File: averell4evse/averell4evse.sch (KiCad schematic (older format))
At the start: 23 parts, among them J1 Conn_01x16, J2 Conn_01x12, J3 Conn_01x04, U1 KT2520K-T, U2 NFCv4, U3 TLC5957RTQ, U4 74AUC1G126, U5 touch_sensor

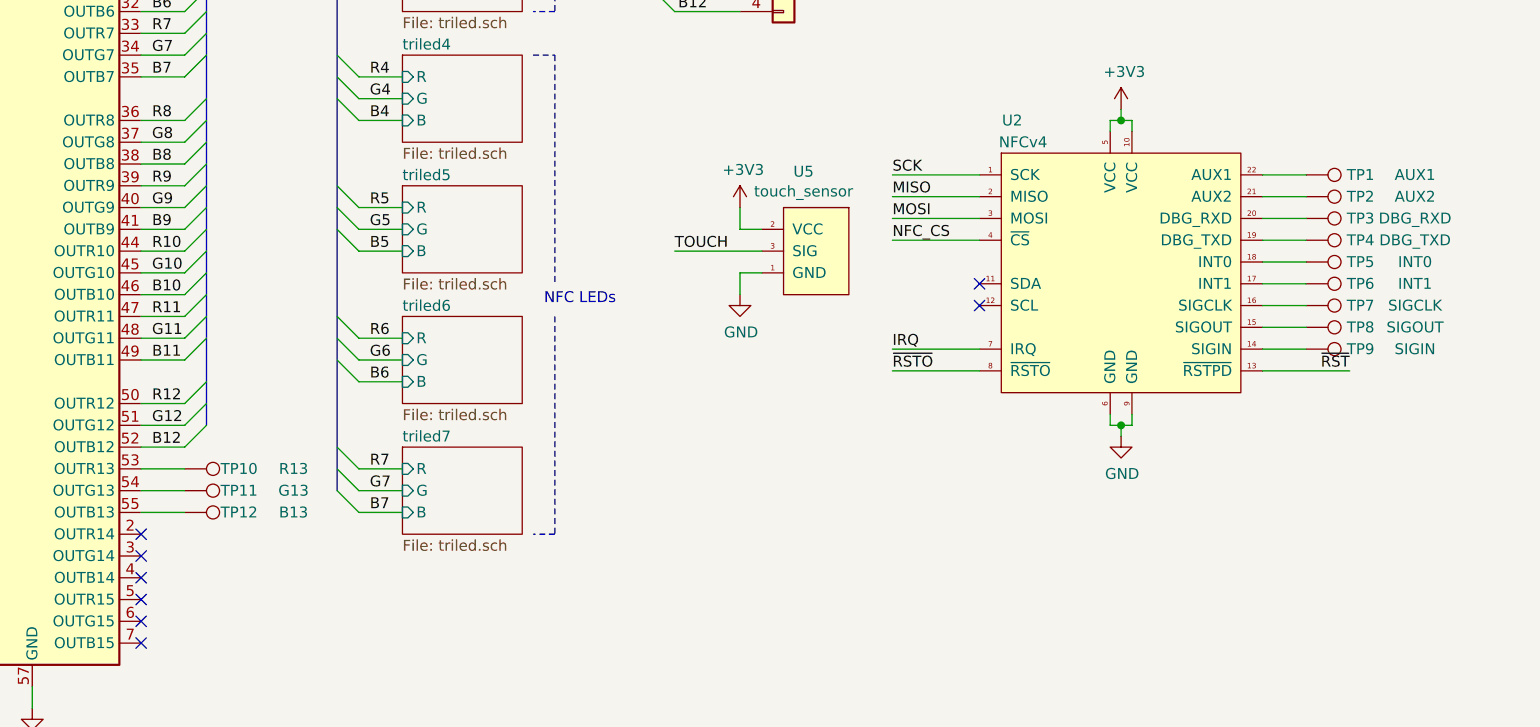
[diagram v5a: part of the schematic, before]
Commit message: averell: Replace test pads with 0.1" pin headers
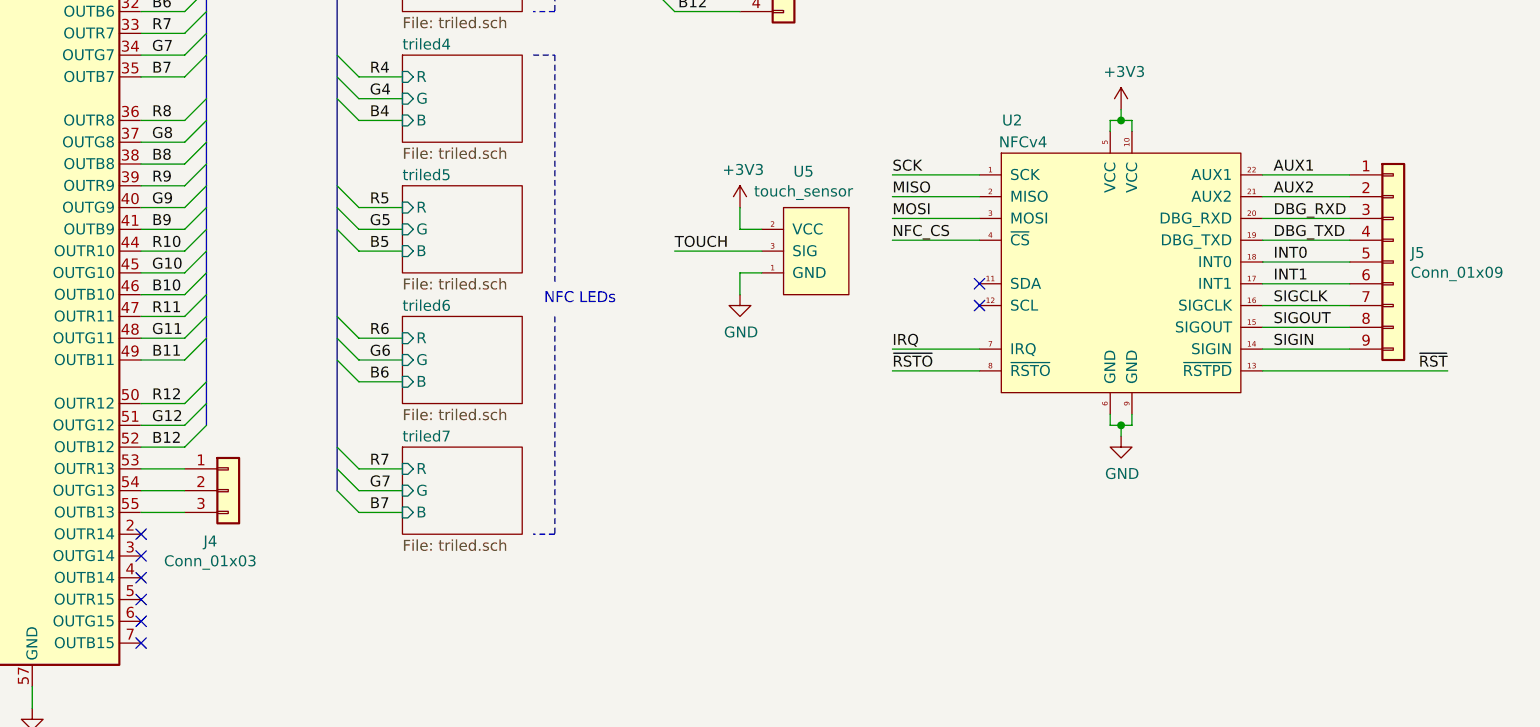
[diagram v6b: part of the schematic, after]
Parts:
- removed TP1: AUX1, TestPoint:TestPoint_THTPad_D1.0mm_Drill0.5mm, symbol Connector:TestPoint
- removed TP10: R13, TestPoint:TestPoint_THTPad_D1.0mm_Drill0.5mm, symbol Connector:TestPoint
- removed TP11: G13, TestPoint:TestPoint_THTPad_D1.0mm_Drill0.5mm, symbol Connector:TestPoint
- removed TP12: B13, TestPoint:TestPoint_THTPad_D1.0mm_Drill0.5mm, symbol Connector:TestPoint
- removed TP2: AUX2, TestPoint:TestPoint_THTPad_D1.0mm_Drill0.5mm, symbol Connector:TestPoint
- removed TP3: DBG_RXD, TestPoint:TestPoint_THTPad_D1.0mm_Drill0.5mm, symbol Connector:TestPoint
- removed TP4: DBG_TXD, TestPoint:TestPoint_THTPad_D1.0mm_Drill0.5mm, symbol Connector:TestPoint
- removed TP5: INT0, TestPoint:TestPoint_THTPad_D1.0mm_Drill0.5mm, symbol Connector:TestPoint
- removed TP6: INT1, TestPoint:TestPoint_THTPad_D1.0mm_Drill0.5mm, symbol Connector:TestPoint
- removed TP7: SIGCLK, TestPoint:TestPoint_THTPad_D1.0mm_Drill0.5mm, symbol Connector:TestPoint
- removed TP8: SIGOUT, TestPoint:TestPoint_THTPad_D1.0mm_Drill0.5mm, symbol Connector:TestPoint
- removed TP9: SIGIN, TestPoint:TestPoint_THTPad_D1.0mm_Drill0.5mm, symbol Connector:TestPoint
- added J4: Conn_01x03, Connector_PinHeader_2.54mm:PinHeader_1x03_P2.54mm_Horizontal, symbol Connector_Generic:Conn_01x03
- added J5: Conn_01x09, Connector_PinHeader_2.54mm:PinHeader_1x09_P2.54mm_Horizontal, symbol Connector_Generic:Conn_01x09
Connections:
- net at U3.53 (OUTR13): now also J4.1 (Pin_1)
- net at U3.54 (OUTG13): now also J4.2 (Pin_2)
- net at U3.55 (OUTB13): now also J4.3 (Pin_3)
- net SIGIN: now reaches U2.14 (SIGIN)
- net SIGIN: now also J5.9 (Pin_9)
- net SIGOUT: now reaches U2.15 (SIGOUT)
- net SIGOUT: now also J5.8 (Pin_8)
- net SIGCLK: now reaches U2.16 (SIGCLK)
- net SIGCLK: now also J5.7 (Pin_7)
- net INT1: now reaches U2.17 (INT1)
- net INT1: now also J5.6 (Pin_6)
- net INT0: now reaches U2.18 (INT0)
- net INT0: now also J5.5 (Pin_5)
- net DBG_TXD: now reaches U2.19 (DBG_TXD)
- net DBG_TXD: now also J5.4 (Pin_4)
- net DBG_RXD: now reaches U2.20 (DBG_RXD)
- net DBG_RXD: now also J5.3 (Pin_3)
- net AUX2: now reaches U2.21 (AUX2)
- net AUX2: now also J5.2 (Pin_2)
- net AUX1: now reaches U2.22 (AUX1)
- net AUX1: now also J5.1 (Pin_1)
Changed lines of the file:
@@
 EESchema Schematic File Version 4
+LIBS:averell4evse-cache
 EELAYER 29 0
 EELAYER END
@@
 	3050 4350 3050 4300
 Wire Wire Line
-	10050 5200 10450 5200
-Text Label 10450 5200 2    50   ~ 0
+	10050 5200 10900 5200
+Text Label 10900 5200 2    50   ~ 0
 ~RST
 $Comp
@@
 The LED driver has no chip select pin,\nthus its SOUT pin never goes high-Z.\nFor a shared MISO, inactive devices must\nput their MISO pin in high-Z, which we\nsimulate here with the buffer chip.
 Wire Wire Line
-	10050 4300 10250 4300
+	10050 4300 10450 4300
 $Comp
 L ma4evse:NFCv4 U2
@@
 	1    0    0    -1
 $EndComp
-$Comp
-L Connector:TestPoint TP1
-U 1 1 5DEAD7B1
-P 10250 4300
-F 0 "TP1" V 10250 4550 50  0000 C CNN
-F 1 "AUX1" V 10250 4800 50  0000 C CNN
-F 2 "TestPoint:TestPoint_THTPad_D1.0mm_Drill0.5mm" H 10450 4300 50  0001 C CNN
-F 3 "~" H 10450 4300 50  0001 C CNN
-	1    10250 4300
-	0    1    1    0
-$EndComp
-Wire Wire Line
-	10050 4400 10250 4400
-$Comp
-L Connector:TestPoint TP2
-U 1 1 5DF04769
-P 10250 4400
-F 0 "TP2" V 10250 4650 50  0000 C CNN
-F 1 "AUX2" V 10250 4900 50  0000 C CNN
-F 2 "TestPoint:TestPoint_THTPad_D1.0mm_Drill0.5mm" H 10450 4400 50  0001 C CNN
-F 3 "~" H 10450 4400 50  0001 C CNN
-	1    10250 4400
-	0    1    1    0
-$EndComp
-Wire Wire Line
-	10050 4500 10250 4500
-$Comp
-L Connector:TestPoint TP3
-U 1 1 5DF0C8F8
-P 10250 4500
-F 0 "TP3" V 10250 4750 50  0000 C CNN
-F 1 "DBG_RXD" V 10250 5000 50  0000 C CNN
-F 2 "TestPoint:TestPoint_THTPad_D1.0mm_Drill0.5mm" H 10450 4500 50  0001 C CNN
-F 3 "~" H 10450 4500 50  0001 C CNN
-	1    10250 4500
-	0    1    1    0
-$EndComp
-Wire Wire Line
-	10050 4600 10250 4600
-$Comp
-L Connector:TestPoint TP4
-U 1 1 5DF14B53
-P 10250 4600
-F 0 "TP4" V 10250 4850 50  0000 C CNN
-F 1 "DBG_TXD" V 10250 5100 50  0000 C CNN
-F 2 "TestPoint:TestPoint_THTPad_D1.0mm_Drill0.5mm" H 10450 4600 50  0001 C CNN
-F 3 "~" H 10450 4600 50  0001 C CNN
-	1    10250 4600
-	0    1    1    0
-$EndComp
-Wire Wire Line
-	10050 4700 10250 4700
-$Comp
-L Connector:TestPoint TP5
-U 1 1 5DF1CF0D
-P 10250 4700
-F 0 "TP5" V 10250 4950 50  0000 C CNN
-F 1 "INT0" V 10250 5200 50  0000 C CNN
-F 2 "TestPoint:TestPoint_THTPad_D1.0mm_Drill0.5mm" H 10450 4700 50  0001 C CNN
-F 3 "~" H 10450 4700 50  0001 C CNN
-	1    10250 4700
-	0    1    1    0
-$EndComp
-Wire Wire Line
-	10050 4800 10250 4800
-$Comp
-L Connector:TestPoint TP6
-U 1 1 5DF253F3
-P 10250 4800
-F 0 "TP6" V 10250 5050 50  0000 C CNN
-F 1 "INT1" V 10250 5300 50  0000 C CNN
-F 2 "TestPoint:TestPoint_THTPad_D1.0mm_Drill0.5mm" H 10450 4800 50  0001 C CNN
-F 3 "~" H 10450 4800 50  0001 C CNN
-	1    10250 4800
-	0    1    1    0
-$EndComp
-Wire Wire Line
-	10050 4900 10250 4900
-$Comp
-L Connector:TestPoint TP7
-U 1 1 5DF2DAFE
-P 10250 4900
-F 0 "TP7" V 10250 5150 50  0000 C CNN
-F 1 "SIGCLK" V 10250 5400 50  0000 C CNN
-F 2 "TestPoint:TestPoint_THTPad_D1.0mm_Drill0.5mm" H 10450 4900 50  0001 C CNN
-F 3 "~" H 10450 4900 50  0001 C CNN
-	1    10250 4900
-	0    1    1    0
-$EndComp
-Wire Wire Line
-	10050 5000 10250 5000
-$Comp
-L Connector:TestPoint TP8
-U 1 1 5DF363A1
-P 10250 5000
-F 0 "TP8" V 10250 5250 50  0000 C CNN
-F 1 "SIGOUT" V 10250 5500 50  0000 C CNN
-F 2 "TestPoint:TestPoint_THTPad_D1.0mm_Drill0.5mm" H 10450 5000 50  0001 C CNN
-F 3 "~" H 10450 5000 50  0001 C CNN
-	1    10250 5000
-	0    1    1    0
-$EndComp
-Wire Wire Line
-	10050 5100 10250 5100
-$Comp
-L Connector:TestPoint TP9
-U 1 1 5DF3ED31
-P 10250 5100
-F 0 "TP9" V 10250 5350 50  0000 C CNN
-F 1 "SIGIN" V 10250 5600 50  0000 C CNN
-F 2 "TestPoint:TestPoint_THTPad_D1.0mm_Drill0.5mm" H 10450 5100 50  0001 C CNN
-F 3 "~" H 10450 5100 50  0001 C CNN
-	1    10250 5100
-	0    1    1    0
-$EndComp
+Wire Wire Line
+	10050 4400 10450 4400
+Wire Wire Line
+	10050 4500 10450 4500
+Wire Wire Line
+	10050 4600 10450 4600
+Wire Wire Line
+	10050 4700 10450 4700
+Wire Wire Line
+	10050 4800 10450 4800
+Wire Wire Line
+	10050 4900 10450 4900
+Wire Wire Line
+	10050 5000 10450 5000
+Wire Wire Line
+	10050 5100 10450 5100
 Wire Wire Line
 	4900 5650 5100 5650
-$Comp
-L Connector:TestPoint TP10
-U 1 1 5DF480E2
-P 5100 5650
-F 0 "TP10" V 5100 5900 50  0000 C CNN
-F 1 "R13" V 5100 6150 50  0000 C CNN
-F 2 "TestPoint:TestPoint_THTPad_D1.0mm_Drill0.5mm" H 5300 5650 50  0001 C CNN
-F 3 "~" H 5300 5650 50  0001 C CNN
-	1    5100 5650
-	0    1    1    0
-$EndComp
 Wire Wire Line
 	4900 5750 5100 5750
-$Comp
-L Connector:TestPoint TP11
-U 1 1 5DF480E9
-P 5100 5750
-F 0 "TP11" V 5100 6000 50  0000 C CNN
-F 1 "G13" V 5100 6250 50  0000 C CNN
-F 2 "TestPoint:TestPoint_THTPad_D1.0mm_Drill0.5mm" H 5300 5750 50  0001 C CNN
-F 3 "~" H 5300 5750 50  0001 C CNN
-	1    5100 5750
-	0    1    1    0
-$EndComp
 Wire Wire Line
 	4900 5850 5100 5850
-$Comp
-L Connector:TestPoint TP12
-U 1 1 5DF480F0
-P 5100 5850
-F 0 "TP12" V 5100 6100 50  0000 C CNN
-F 1 "B13" V 5100 6350 50  0000 C CNN
-F 2 "TestPoint:TestPoint_THTPad_D1.0mm_Drill0.5mm" H 5300 5850 50  0001 C CNN
-F 3 "~" H 5300 5850 50  0001 C CNN
-	1    5100 5850
-	0    1    1    0
-$EndComp
 $Sheet
 S 6100 1950 550  400
@@
 	1    0    0    -1
 $EndComp
+$Comp
+L Connector_Generic:Conn_01x03 J4
+U 1 1 5DDA55B8
+P 5300 5750
+F 0 "J4" H 5218 5517 50  0000 C CNN
+F 1 "Conn_01x03" H 5218 5426 50  0000 C CNN
+F 2 "Connector_PinHeader_2.54mm:PinHeader_1x03_P2.54mm_Horizontal" H 5300 5750 50  0001 C CNN
+F 3 "~" H 5300 5750 50  0001 C CNN
+	1    5300 5750
+	1    0    0    -1
+$EndComp
+$Comp
+L Connector_Generic:Conn_01x09 J5
+U 1 1 5DDB2582
+P 10650 4700
+F 0 "J5" H 10730 4742 50  0000 L CNN
+F 1 "Conn_01x09" H 10730 4651 50  0000 L CNN
+F 2 "Connector_PinHeader_2.54mm:PinHeader_1x09_P2.54mm_Horizontal" H 10650 4700 50  0001 C CNN
+F 3 "~" H 10650 4700 50  0001 C CNN
+	1    10650 4700
+	1    0    0    -1
+$EndComp
+Text Label 10100 4300 0    50   ~ 0
+AUX1
+Text Label 10100 4400 0    50   ~ 0
+AUX2
+Text Label 10100 4500 0    50   ~ 0
+DBG_RXD
+Text Label 10100 4600 0    50   ~ 0
+DBG_TXD
+Text Label 10100 4700 0    50   ~ 0
+INT0
+Text Label 10100 4800 0    50   ~ 0
+INT1
+Text Label 10100 4900 0    50   ~ 0
+SIGCLK
+Text Label 10100 5000 0    50   ~ 0
+SIGOUT
+Text Label 10100 5100 0    50   ~ 0
+SIGIN
 Wire Bus Line
 	7250 1050 7250 3450

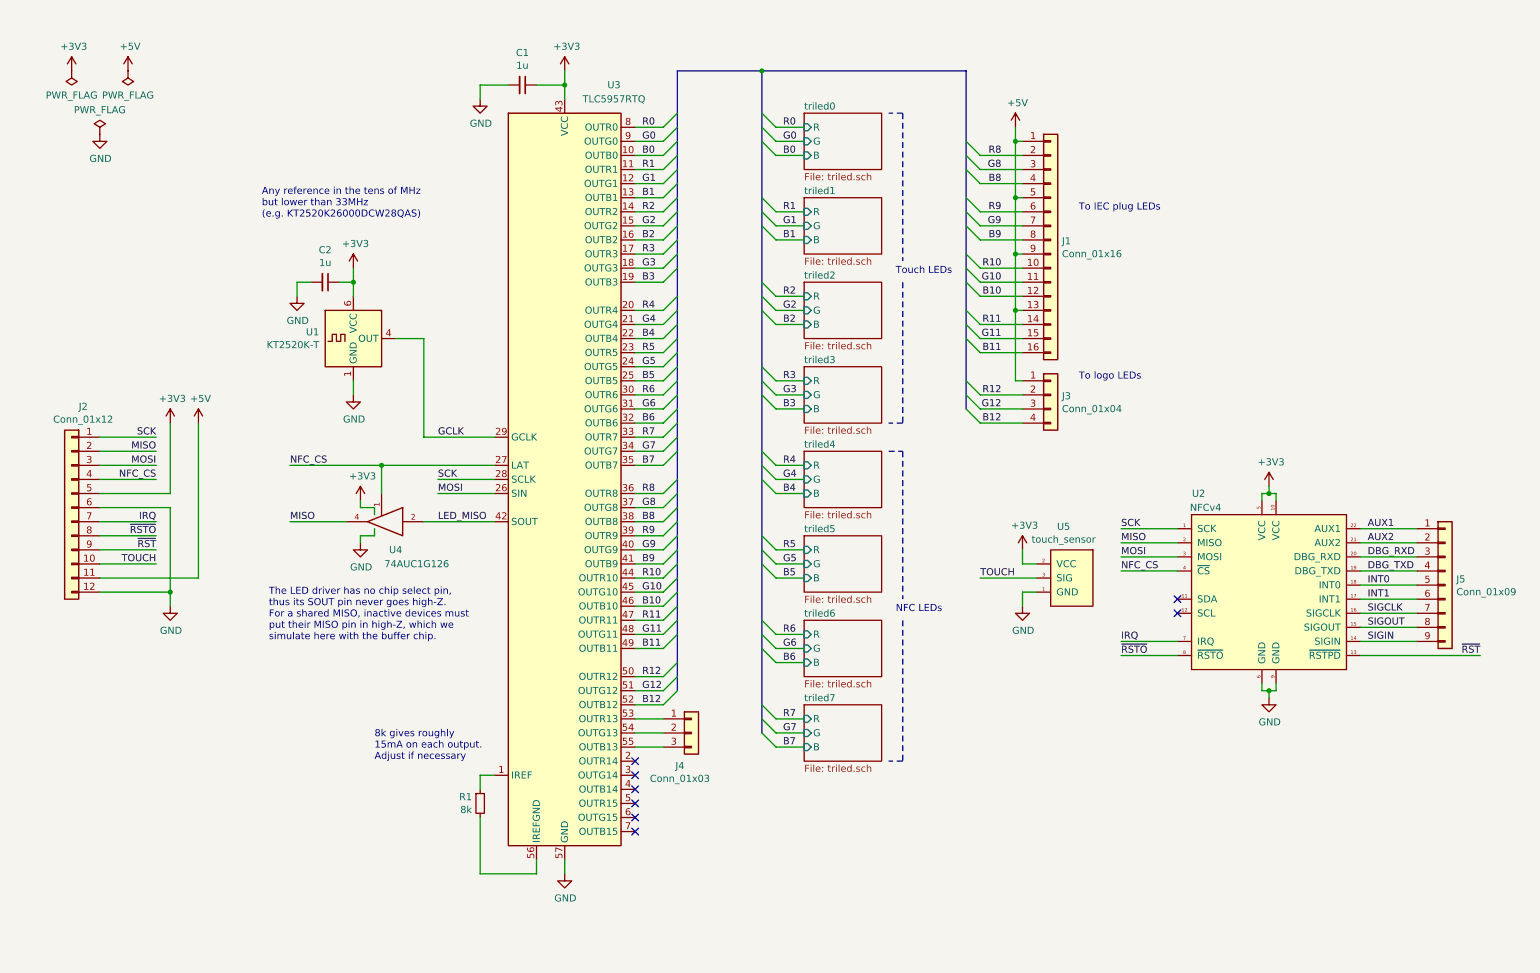
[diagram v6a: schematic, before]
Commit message: averell/*: Make a real CS for LED driver
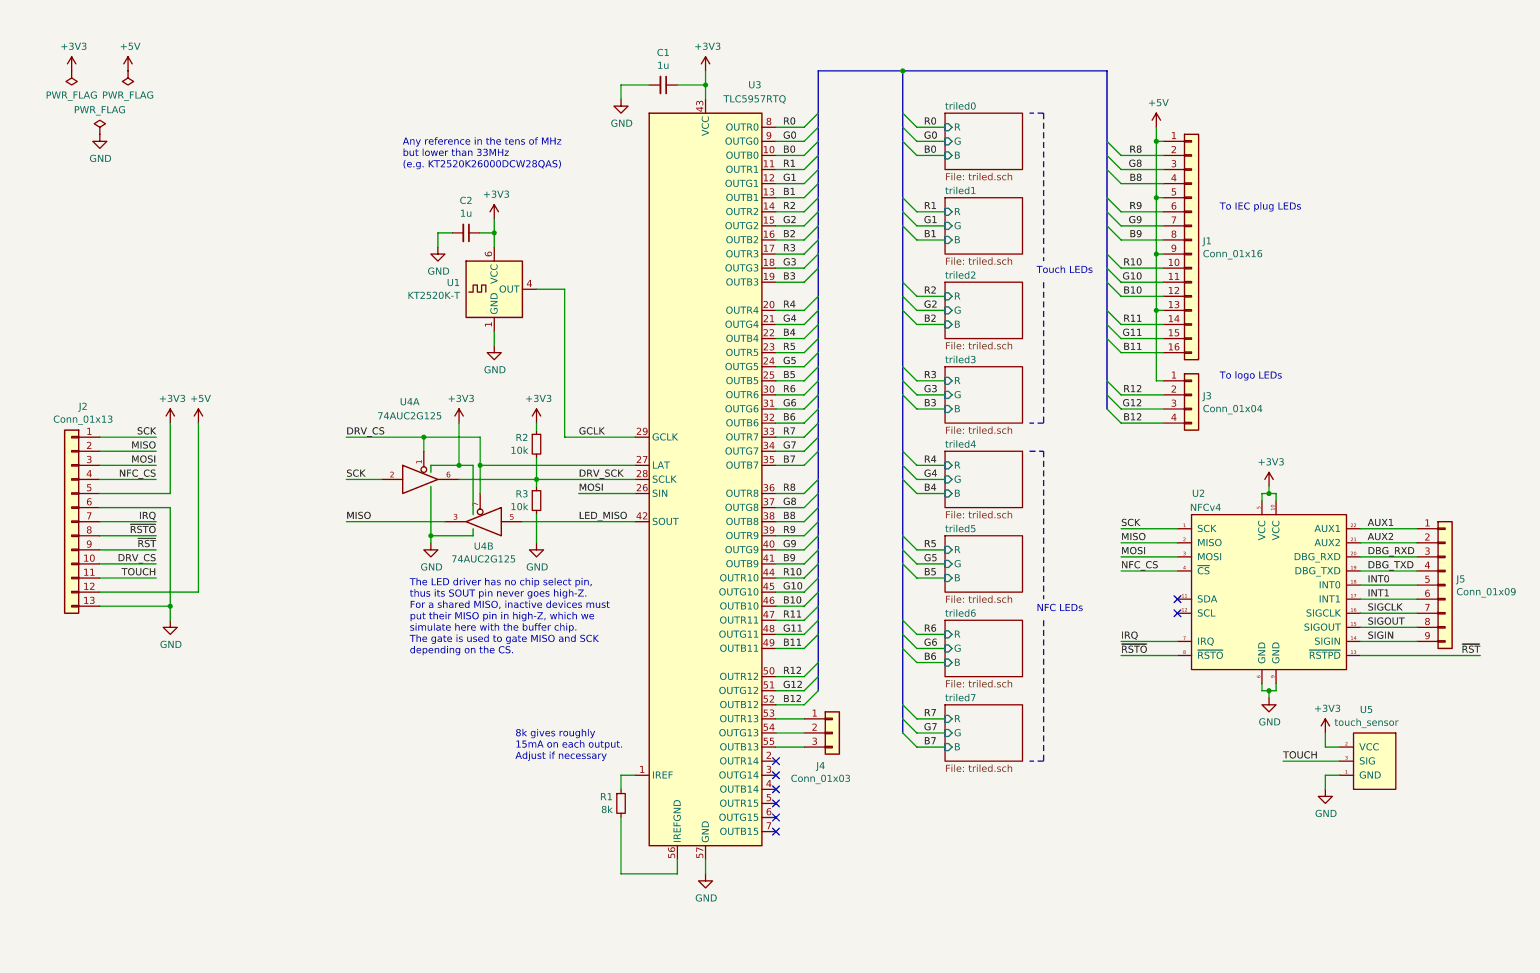
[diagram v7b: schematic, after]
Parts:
- removed J2: Conn_01x12, Connector_PinHeader_2.54mm:PinHeader_1x12_P2.54mm_Horizontal, symbol Connector_Generic:Conn_01x12
- removed U4: 74AUC1G126, Package_TO_SOT_SMD:SOT-23-5, symbol 74xGxx:74AUC1G126
- added J2: Conn_01x13, Connector_PinHeader_2.54mm:PinHeader_1x13_P2.54mm_Horizontal, symbol Connector_Generic:Conn_01x13
- added R2, R3: 10k, Resistor_SMD:R_0603_1608Metric, symbol Device:R_Small
- added U4: 74AUC2G125, Package_SO:TSSOP-8_3x3mm_P0.65mm, symbol 74xGxx:74AUC2G125
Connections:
- net +3V3: now also J2.5 (Pin_5), R2.1, U4.8 (VCC), U4.8 (VCC)
- net +5V: now also J2.12 (Pin_12)
- net GND: now also J2.13 (Pin_13), J2.6 (Pin_6), R3.2, U4.4 (GND), U4.4 (GND)
- net IRQ: now also J2.7 (Pin_7)
- net LED_MISO: now also U4.5
- net MISO: now also J2.2 (Pin_2), U4.3
- net MOSI: now also J2.3 (Pin_3)
- net NFC_CS: now also J2.4 (Pin_4); no longer U3.27 (LAT)
- net SCK: now also J2.1 (Pin_1), U4.2; no longer U3.28 (SCLK)
- net TOUCH: now also J2.11 (Pin_11)
- net ~RST: now also J2.9 (Pin_9)
- net ~RSTO: now also J2.8 (Pin_8)
- new net DRV_CS: J2.10 (Pin_10), U3.27 (LAT), U4.1, U4.7
- new net DRV_SCK: R2.2, R3.1, U3.28 (SCLK), U4.6
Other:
- note added: "The LED driver has no chip select pin,\nthus its SOUT pin never goes high-Z.\nFor a shared MISO, inactive devices must\nput their MISO pin in high-Z, which we\nsimulate here with the buffer chip.\nThe gate is used to gate MISO and SCK\ndepending on the CS."
- note removed: "The LED driver has no chip select pin,\nthus its SOUT pin never goes high-Z.\nFor a shared MISO, inactive devices must\nput their MISO pin in high-Z, which we\nsimulate here with the buffer chip."
- moved on the sheet: C1, C2, J1, J3, J4, R1, U1, U3, U5
